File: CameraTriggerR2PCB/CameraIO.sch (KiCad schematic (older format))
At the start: 13 parts, among them J1 Camera 3.5mm, J2 Camera 2.5mm, Q1 PN2222A, Q2 PN2222A, U1 ILD74, U2 ILD74

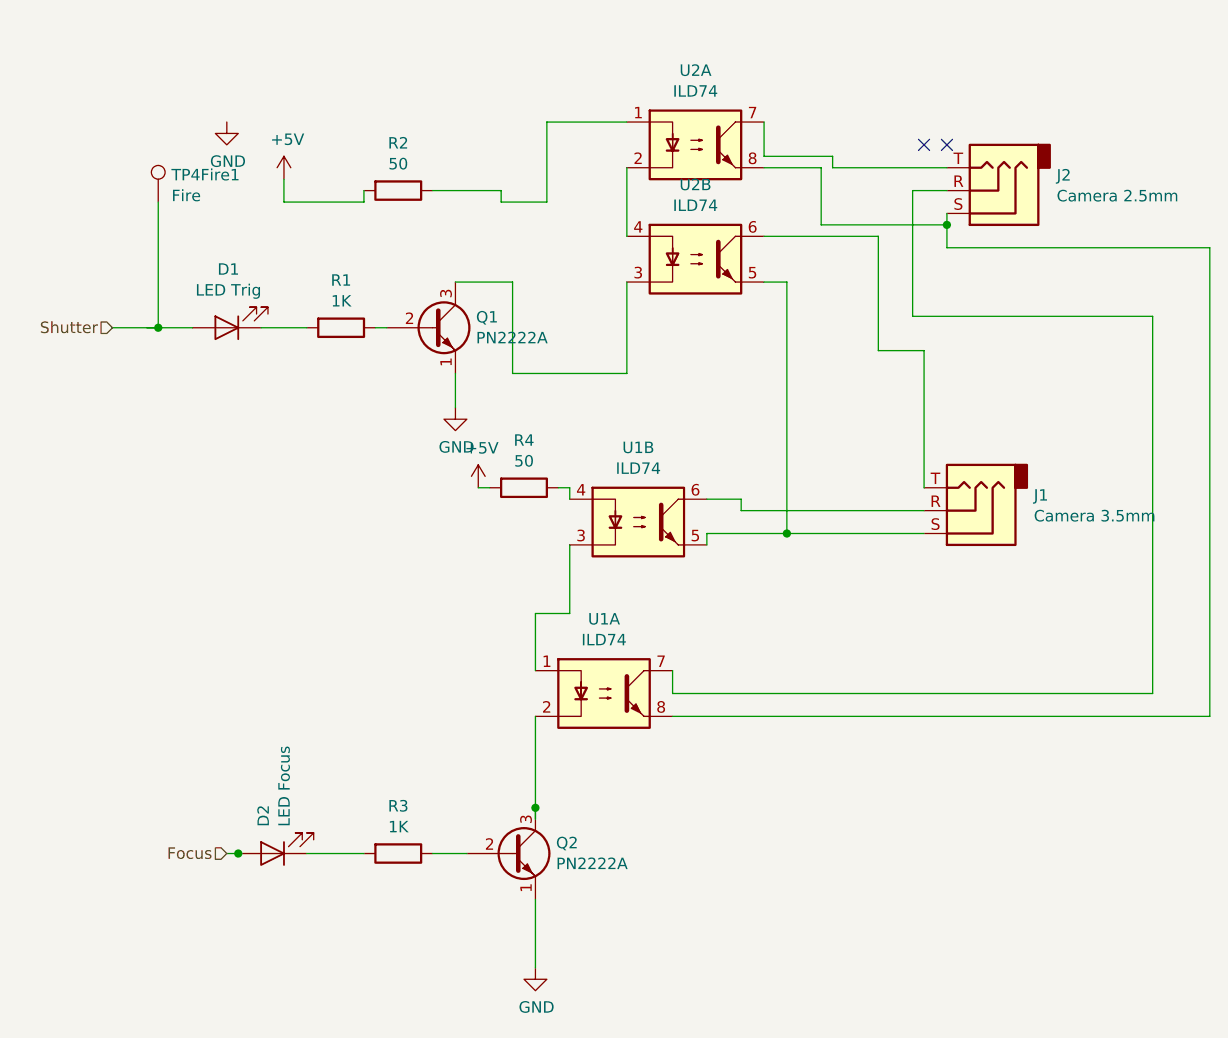
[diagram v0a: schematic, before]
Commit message: Add files via upload
Adding XLR connector
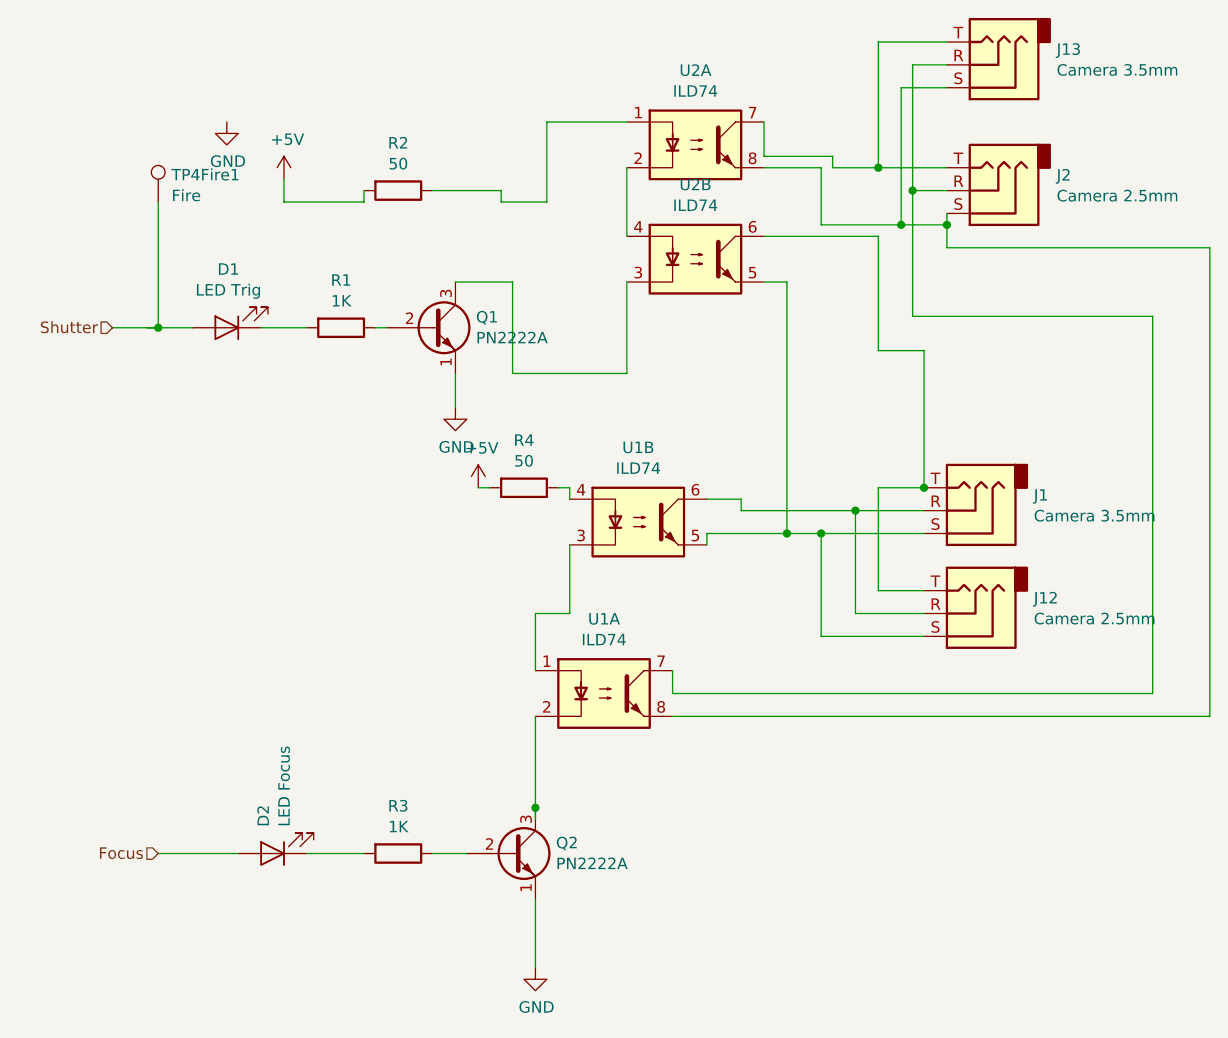
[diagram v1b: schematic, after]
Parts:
- added J12: Camera 2.5mm, CameraTriggerPCB:CUI_SJ1-2503A, symbol Connector:AudioJack3
- added J13: Camera 3.5mm, Connector_Audio:Jack_3.5mm_CUI_SJ1-3533NG_Horizontal_CircularHoles, symbol Connector:AudioJack3
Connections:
- wire segments 62 -> 79
- no-connect marks 2 -> 0
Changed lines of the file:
@@
 $Descr A4 11693 8268
 encoding utf-8
-Sheet 2 8
+Sheet 2 9
 Title ""
 Date ""
@@
 $EndComp
 $Comp
-L Device:LED D?
-U 1 1 5ECCF3A5
-P 3150 2900
-AR Path="/5ECCF3A5" Ref="D?"  Part="1"
-AR Path="/5EBC562C/5ECCF3A5" Ref="D1"  Part="1"
-F 0 "D1" H 3143 2645 50  0000 C CNN
-F 1 "LED Trig" H 3143 2736 50  0000 C CNN
-F 2 "LED_THT:LED_D3.0mm" H 3150 2900 50  0001 C CNN
-F 3 "~" H 3150 2900 50  0001 C CNN
-	1    3150 2900
-	-1   0    0    1
-$EndComp
-$Comp
 L Device:R R?
 U 1 1 5ECCF3AB
@@
 	6200 3600 6200 3000
 Wire Wire Line
-	5600 3800 6200 3800
-$Comp
-L Connector:AudioJack3 J?
-U 1 1 5ECCF3B4
-P 6500 2300
-AR Path="/5ECCF3B4" Ref="J?"  Part="1"
-AR Path="/5EBC562C/5ECCF3B4" Ref="J2"  Part="1"
-F 0 "J2" H 6220 2233 50  0000 R CNN
-F 1 "Camera 2.5mm" H 6220 2324 50  0000 R CNN
-F 2 "CameraTriggerPCB:CUI_SJ1-2503A" H 6500 2300 50  0001 C CNN
-F 3 "~" H 6500 2300 50  0001 C CNN
-	1    6500 2300
-	-1   0    0    1
-$EndComp
+	5600 3800 5750 3800
 Wire Wire Line
 	7200 4500 7200 2850
@@
 Wire Wire Line
 	6150 2850 6150 2300
-Wire Wire Line
-	6150 2300 6300 2300
 Wire Wire Line
 	7450 4600 7450 2550
@@
 	4550 2350 4350 2350
 Wire Wire Line
-	6300 2450 5750 2450
+	6300 2450 6100 2450
 Wire Wire Line
 	5750 2450 5750 2200
@@
 $EndComp
 Wire Wire Line
-	6200 3700 5400 3700
+	6200 3700 5900 3700
 Wire Wire Line
 	5400 3700 5400 3650
@@
 	3300 2900 3500 2900
 $Comp
+L Connector:TestPoint TP4Fire?
+U 1 1 5ECCF444
+P 2850 2350
+AR Path="/5ECCF444" Ref="TP4Fire?"  Part="1"
+AR Path="/5EBC562C/5ECCF444" Ref="TP4Fire1"  Part="1"
+F 0 "TP4Fire1" H 2908 2468 50  0000 L CNN
+F 1 "Fire" H 2908 2377 50  0000 L CNN
+F 2 "TestPoint:TestPoint_Keystone_5010-5014_Multipurpose" H 3050 2350 50  0001 C CNN
+F 3 "~" H 3050 2350 50  0001 C CNN
+	1    2850 2350
+	1    0    0    -1
+$EndComp
+Wire Wire Line
+	5800 2200 5800 2150
+Wire Wire Line
+	5800 2150 5500 2150
+Wire Wire Line
+	5500 2150 5500 2000
+Text HLabel 2850 5200 0    50   Input ~ 0
+Focus
+Text HLabel 2650 2900 0    50   Input ~ 0
+Shutter
+Wire Wire Line
+	2650 2900 2850 2900
+Wire Wire Line
+	2800 2900 2850 2900
+Wire Wire Line
+	2850 2900 3000 2900
+Connection ~ 2850 2900
+Wire Wire Line
+	2850 2350 2850 2900
+$Comp
+L Device:LED D?
+U 1 1 5ECCF3A5
+P 3150 2900
+AR Path="/5ECCF3A5" Ref="D?"  Part="1"
+AR Path="/5EBC562C/5ECCF3A5" Ref="D1"  Part="1"
+F 0 "D1" H 3143 2645 50  0000 C CNN
+F 1 "LED Trig" H 3143 2736 50  0000 C CNN
+F 2 "LED_THT:LED_D3.0mm" H 3150 2900 50  0001 C CNN
+F 3 "~" H 3150 2900 50  0001 C CNN
+	1    3150 2900
+	-1   0    0    1
+$EndComp
+$Comp
+L Connector:AudioJack3 J?
+U 1 1 5EC210E3
+P 6400 4150
+AR Path="/5EC210E3" Ref="J?"  Part="1"
+AR Path="/5EBC562C/5EC210E3" Ref="J12"  Part="1"
+F 0 "J12" H 6120 4083 50  0000 R CNN
+F 1 "Camera 2.5mm" H 6120 4174 50  0000 R CNN
+F 2 "CameraTriggerPCB:CUI_SJ1-2503A" H 6400 4150 50  0001 C CNN
+F 3 "~" H 6400 4150 50  0001 C CNN
+	1    6400 4150
+	-1   0    0    1
+$EndComp
+$Comp
+L Connector:AudioJack3 J?
+U 1 1 5EC230DE
+P 6500 1750
+AR Path="/5EC230DE" Ref="J?"  Part="1"
+AR Path="/5EBC562C/5EC230DE" Ref="J13"  Part="1"
+F 0 "J13" H 6220 1683 50  0000 R CNN
+F 1 "Camera 3.5mm" H 6220 1774 50  0000 R CNN
+F 2 "Connector_Audio:Jack_3.5mm_CUI_SJ1-3533NG_Horizontal_CircularHoles" H 6500 1750 50  0001 C CNN
+F 3 "~https://www.mouser.com/datasheet/2/670/sj1-353xng-1313133.pdf" H 6500 1750 50  0001 C CNN
+	1    6500 1750
+	-1   0    0    1
+$EndComp
+Wire Wire Line
+	6200 4050 6000 4050
+Wire Wire Line
+	6000 4050 6000 3600
+Wire Wire Line
+	6000 3600 6200 3600
+Connection ~ 6200 3600
+Wire Wire Line
+	5900 4150 5900 3700
+Connection ~ 5900 3700
+Wire Wire Line
+	5900 3700 5400 3700
+Wire Wire Line
+	6200 4250 5750 4250
+Wire Wire Line
+	5750 4250 5750 3800
+Connection ~ 5750 3800
+Wire Wire Line
+	5750 3800 6200 3800
+Wire Wire Line
+	5900 4150 6200 4150
+Wire Wire Line
+	6150 2300 6300 2300
+Wire Wire Line
+	6300 2200 6000 2200
+$Comp
+L Connector:AudioJack3 J?
+U 1 1 5ECCF3B4
+P 6500 2300
+AR Path="/5ECCF3B4" Ref="J?"  Part="1"
+AR Path="/5EBC562C/5ECCF3B4" Ref="J2"  Part="1"
+F 0 "J2" H 6220 2233 50  0000 R CNN
+F 1 "Camera 2.5mm" H 6220 2324 50  0000 R CNN
+F 2 "CameraTriggerPCB:CUI_SJ1-2503A" H 6500 2300 50  0001 C CNN
+F 3 "~" H 6500 2300 50  0001 C CNN
+	1    6500 2300
+	-1   0    0    1
+$EndComp
+Wire Wire Line
+	6300 1850 6100 1850
+Wire Wire Line
+	6100 1850 6100 2450
+Connection ~ 6100 2450
+Wire Wire Line
+	6100 2450 5750 2450
+Wire Wire Line
+	6150 2300 6150 1750
+Wire Wire Line
+	6150 1750 6300 1750
+Connection ~ 6150 2300
+Wire Wire Line
+	6000 2200 6000 1650
+Wire Wire Line
+	6000 1650 6300 1650
+Connection ~ 6000 2200
+Wire Wire Line
+	6000 2200 5800 2200
+$Comp
 L Device:LED D?
 U 1 1 5ECCF43E
@@
 	-1   0    0    1
 $EndComp
-$Comp
-L Connector:TestPoint TP4Fire?
-U 1 1 5ECCF444
-P 2850 2350
-AR Path="/5ECCF444" Ref="TP4Fire?"  Part="1"
-AR Path="/5EBC562C/5ECCF444" Ref="TP4Fire1"  Part="1"
-F 0 "TP4Fire1" H 2908 2468 50  0000 L CNN
-F 1 "Fire" H 2908 2377 50  0000 L CNN
-F 2 "TestPoint:TestPoint_Keystone_5010-5014_Multipurpose" H 3050 2350 50  0001 C CNN
-F 3 "~" H 3050 2350 50  0001 C CNN
-	1    2850 2350
-	1    0    0    -1
-$EndComp
-Wire Wire Line
-	2850 2350 2850 2900
-Connection ~ 2850 2900
-Wire Wire Line
-	3150 5200 3200 5200
-Wire Wire Line
-	2850 2900 3000 2900
-Wire Wire Line
-	2800 2900 2850 2900
-Wire Wire Line
-	2650 2900 2850 2900
-Wire Wire Line
-	6300 2200 5800 2200
-Wire Wire Line
-	5800 2200 5800 2150
-Wire Wire Line
-	5800 2150 5500 2150
-Wire Wire Line
-	5500 2150 5500 2000
-NoConn ~ 6300 2100
-NoConn ~ 6200 2100
-Text HLabel 2650 2900 0    50   Input ~ 0
-Shutter
-Text HLabel 3150 5200 0    50   Input ~ 0
-Focus
-Connection ~ 3200 5200
+Wire Wire Line
+	2850 5200 3200 5200
 $EndSCHEMATC
